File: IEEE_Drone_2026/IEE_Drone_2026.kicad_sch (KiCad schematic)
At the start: 15 parts, among them IC1 TPSM84209RKHT, J1 Conn_01x03_Socket, J2 Conn_01x03_Socket, J3 Conn_01x03_Socket, J4 Conn_01x03_Socket, U1 MS560702BA03-50

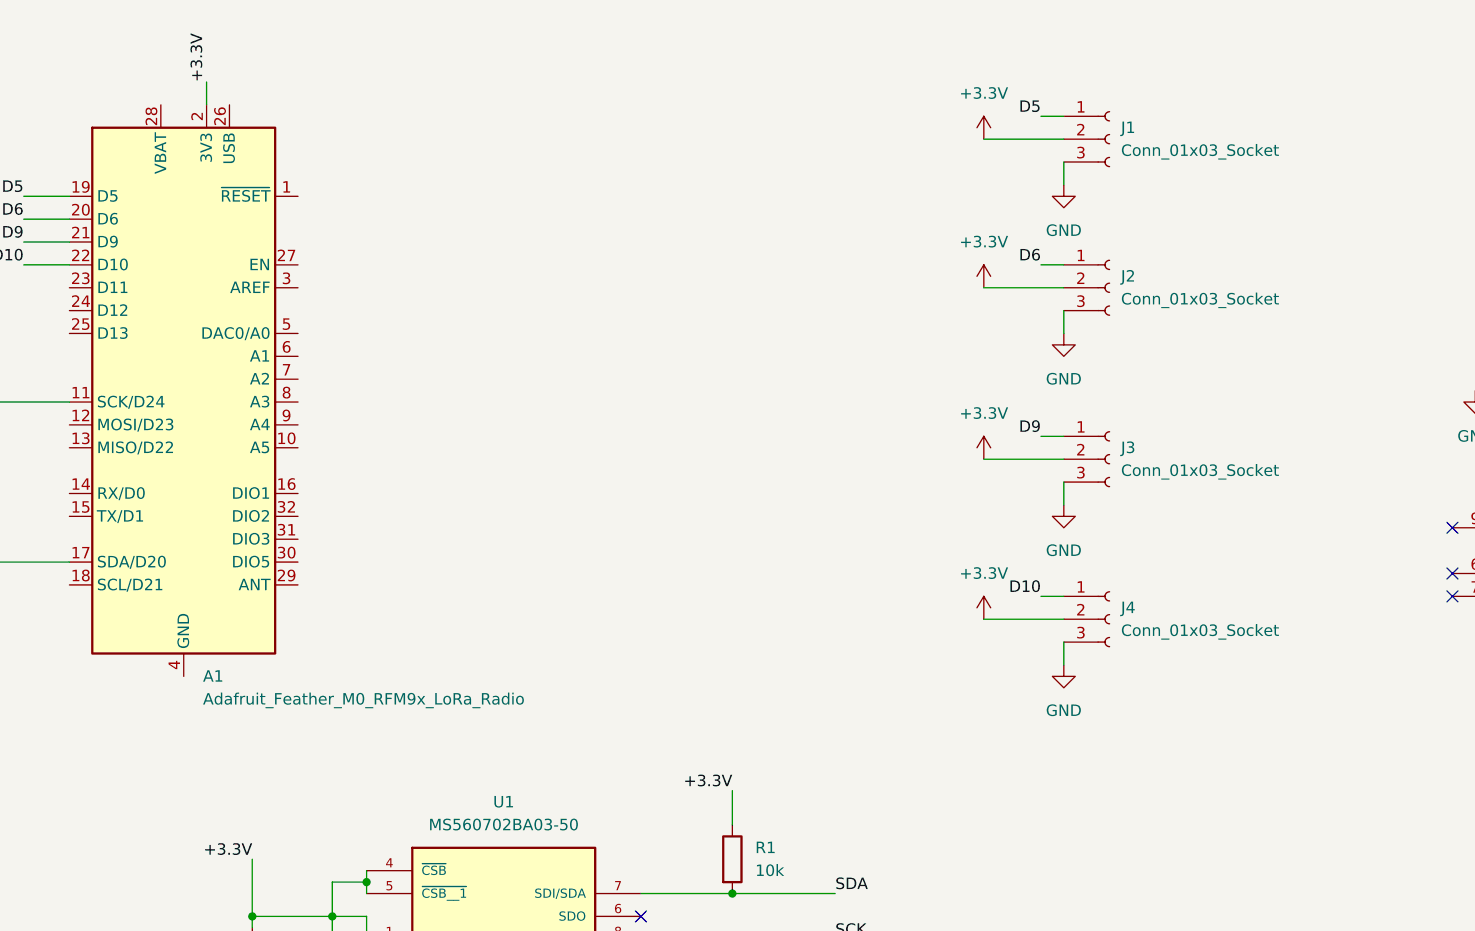
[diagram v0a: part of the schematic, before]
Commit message: redesign of feather system to incorporate ESC system
added mounting pins, changed board size, redesigned pwr system and moved it and barometer, removed individual servo pins and added 1x6 conn for ESC
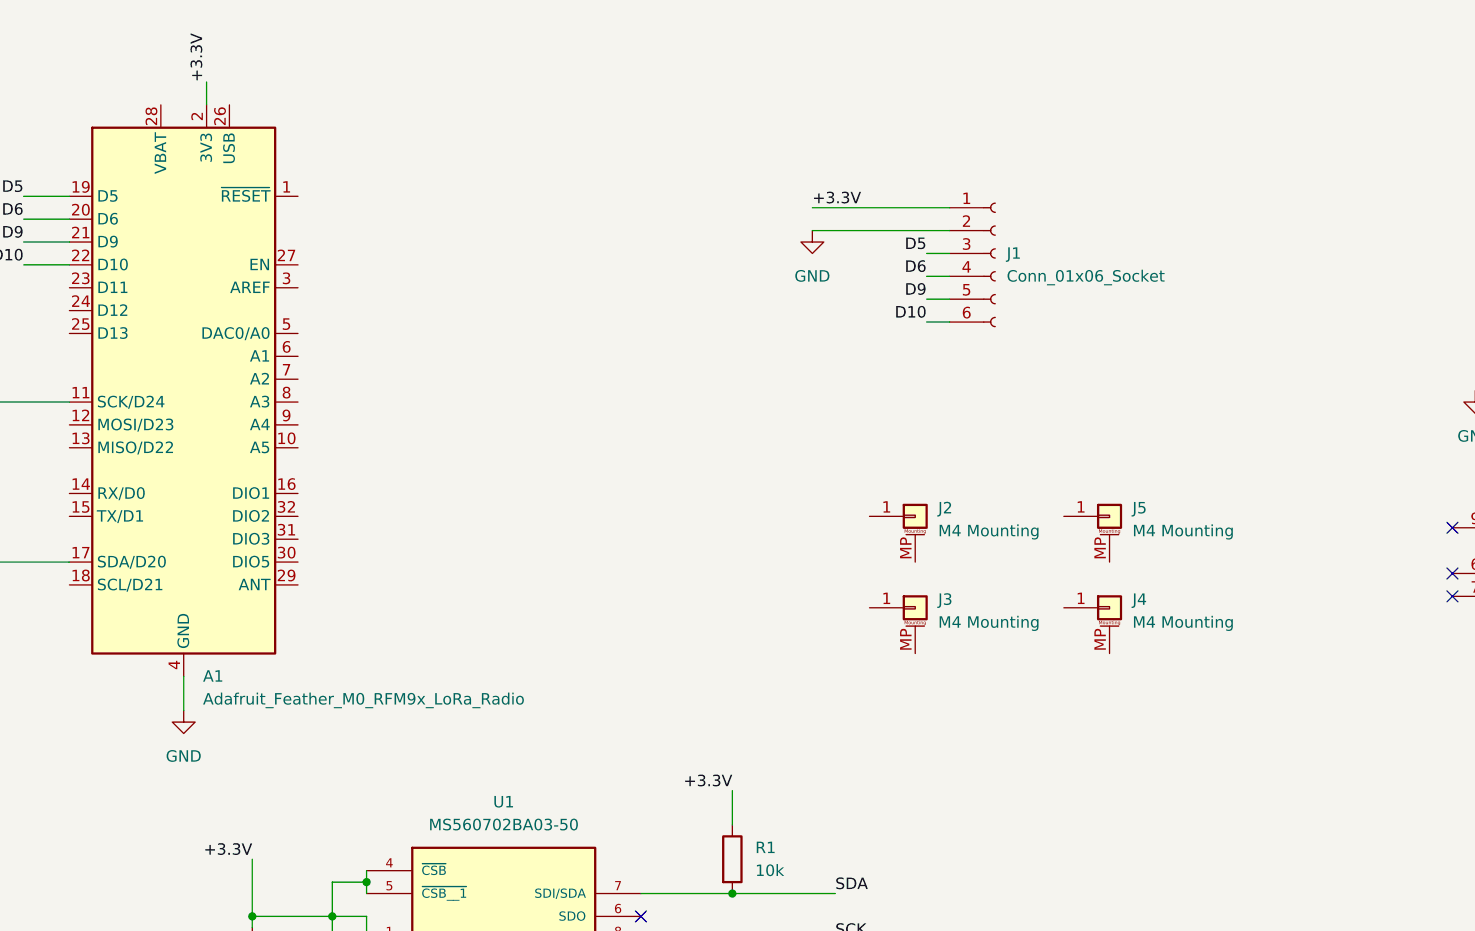
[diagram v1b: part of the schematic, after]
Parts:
- removed J1, J2, J3, J4: Conn_01x03_Socket, Connector_PinSocket_2.54mm:PinSocket_1x03_P2.54mm_Vertical, symbol Connector:Conn_01x03_Socket
- added J1: Conn_01x06_Socket, Connector_PinHeader_1.00mm:PinHeader_1x06_P1.00mm_Vertical, symbol Connector:Conn_01x06_Socket
- added J2, J3, J4, J5: M4 Mounting, Mounting:MountingHole_4.3mm_M4, symbol Connector_Generic_MountingPin:Conn_01x01_MountingPin
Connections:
- net +3.3V: now also J1.1 (Pin_1)
- net D10: now also J1.6 (Pin_6)
- net D5: now also J1.3 (Pin_3)
- net D6: now also J1.4 (Pin_4)
- net D9: now also J1.5 (Pin_5)
- net GND: now also A1.4 (GND), J1.2 (Pin_2)

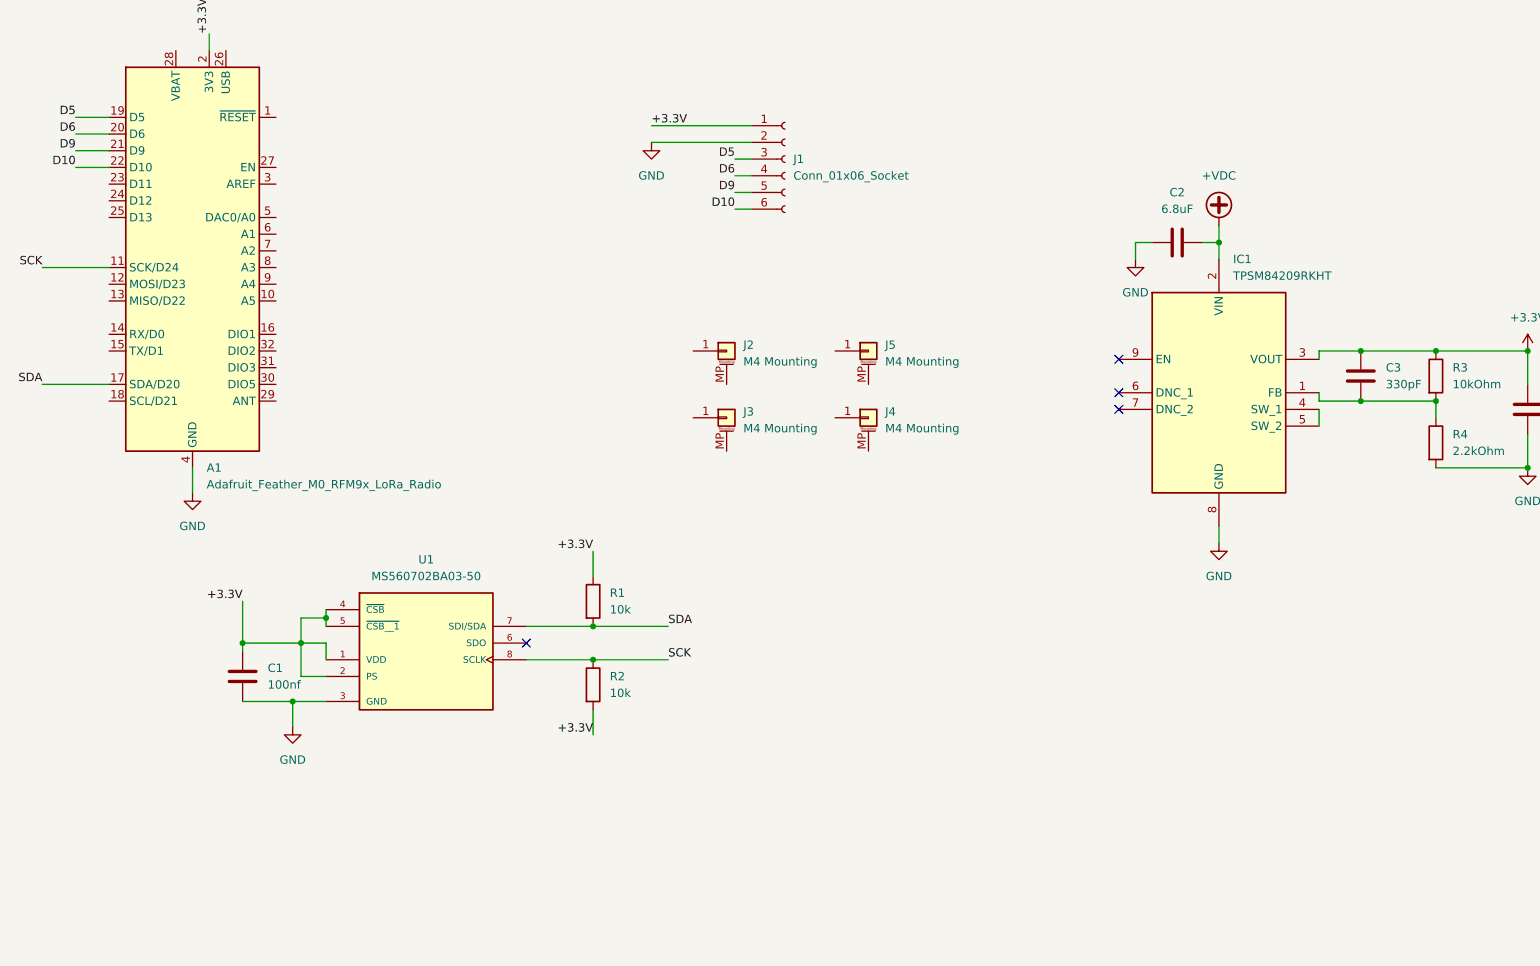
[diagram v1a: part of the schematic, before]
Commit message: added second power regulator for 6v to pixy2m added a couple more labels
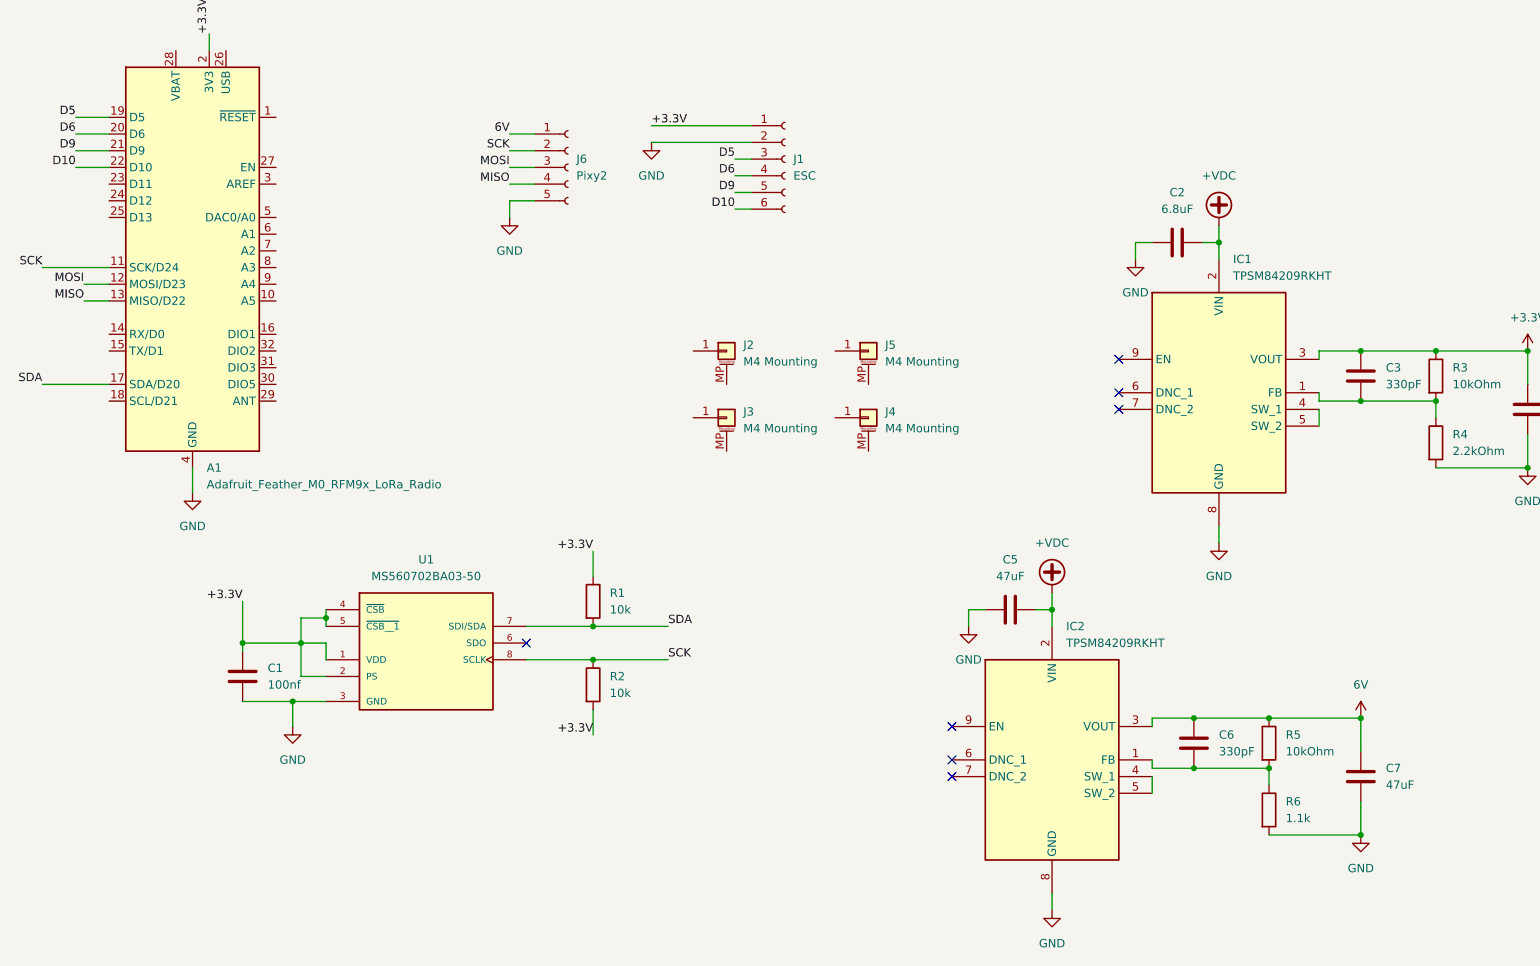
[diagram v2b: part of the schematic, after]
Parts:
- added C5, C7: 47uF, Capacitor_SMD:C_0603_1608Metric_Pad1.08x0.95mm_HandSolder, symbol Device:C
- added C6: 330pF, Capacitor_SMD:C_0603_1608Metric_Pad1.08x0.95mm_HandSolder, symbol Device:C
- added IC2: TPSM84209RKHT, TPSM84209RKHT, symbol TPSM84209RKHT:TPSM84209RKHT
- added J6: Pixy2, Connector_PinSocket_2.54mm:PinSocket_1x05_P2.54mm_Vertical, symbol Connector:Conn_01x05_Socket
- added R5: 10kOhm, Resistor_SMD:R_0603_1608Metric_Pad0.98x0.95mm_HandSolder, symbol Device:R
- added R6: 1.1k, Resistor_SMD:R_0603_1608Metric_Pad0.98x0.95mm_HandSolder, symbol Device:R
- J1: value Conn_01x06_Socket -> ESC
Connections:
- net +VDC: now also C5.2, IC2.2 (VIN)
- net GND: now also C5.1, C7.2, IC2.8 (GND), J6.5 (Pin_5), R6.2
- net SCK: now also J6.2 (Pin_2)
- net MOSI: now reaches A1.12 (MOSI/D23)
- net MOSI: now also J6.3 (Pin_3)
- net MISO: now reaches A1.13 (MISO/D22)
- net MISO: now also J6.4 (Pin_4)
- new net: C6.2, IC2.1 (FB), R5.2, R6.1
- new net: IC2.4 (SW_1), IC2.5 (SW_2)
- new net 6V: C6.1, C7.1, IC2.3 (VOUT), J6.1 (Pin_1), R5.1
- no-connect marks 4 -> 7

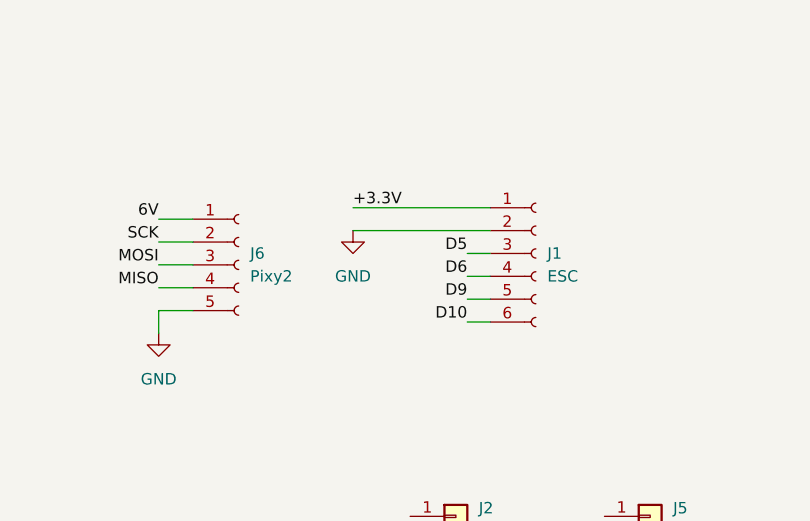
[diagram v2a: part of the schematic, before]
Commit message: updated ESC connector to fix conn issue.
will need to twist the ESC connection cable to properly connect to the ESC
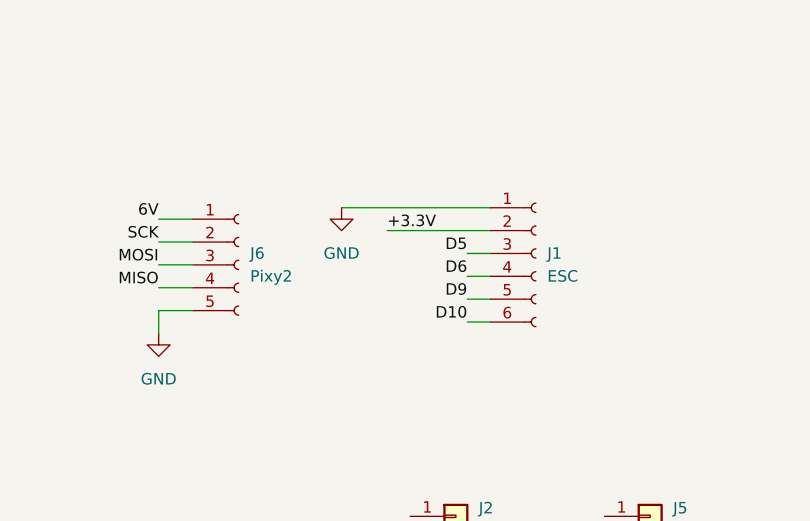
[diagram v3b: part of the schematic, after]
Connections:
- net +3.3V: now also J1.2 (Pin_2); no longer J1.1 (Pin_1)
- net GND: now also J1.1 (Pin_1); no longer J1.2 (Pin_2)
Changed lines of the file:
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@@
+	(wire
+		(pts
+			(xy 146.05 38.1) (xy 157.48 38.1)
+		)
+		(stroke
+			(width 0)
+			(type default)
+		)
+	)
 	(wire
 		(pts
@@
 	(wire
 		(pts
-			(xy 142.24 38.1) (xy 157.48 38.1)
-		)
-		(stroke
-			(width 0)
-			(type default)
-		)
-	)
-	(wire
-		(pts
 			(xy 120.65 46.99) (xy 124.46 46.99)
 		)
@@
 	(wire
 		(pts
+			(xy 140.97 35.56) (xy 157.48 35.56)
+		)
+		(stroke
+			(width 0)
+			(type default)
+		)
+	)
+	(wire
+		(pts
 			(xy 72.39 87.63) (xy 72.39 91.44)
 		)
@@
 		(pts
 			(xy 133.35 111.76) (xy 144.78 111.76)
-		)
-		(stroke
-			(width 0)
-			(type default)
-		)
-	)
-	(wire
-		(pts
-			(xy 142.24 35.56) (xy 157.48 35.56)
 		)
 		(stroke
@@
 	)
 	(label "+3.3V"
-		(at 142.24 35.56 0)
+		(at 146.05 38.1 0)
 		(effects
 			(font
@@
 	(symbol
 		(lib_id "power:GND")
-		(at 142.24 38.1 0)
+		(at 140.97 35.56 0)
 		(unit 1)
 		(exclude_from_sim no)
@@
 		(fields_autoplaced yes)
 		(property "Reference" "#PWR02"
-			(at 142.24 44.45 0)
+			(at 140.97 41.91 0)
 			(effects
 				(font
@@
 		)
 		(property "Value" "GND"
-			(at 142.24 43.18 0)
+			(at 140.97 40.64 0)
 			(effects
 				(font
@@
 		)
 		(property "Footprint" ""
-			(at 142.24 38.1 0)
+			(at 140.97 35.56 0)
 			(effects
 				(font
@@
 		)
 		(property "Datasheet" ""
-			(at 142.24 38.1 0)
+			(at 140.97 35.56 0)
 			(effects
 				(font
@@
 		)
 		(property "Description" "Power symbol creates a global label with name \"GND\" , ground"
-			(at 142.24 38.1 0)
-			(effects
-				(font
+			(at 140.97 35.56 0)
+			(effects
+				(font

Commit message: added crappy mounting holes. probably need to redo
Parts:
- added J10, J7, J8, J9: M2, MountingHole:MountingHole_2.2mm_M2, symbol Connector_Generic_MountingPin:Conn_01x01_MountingPin
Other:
- moved on the sheet: J2, J3, J4, J5

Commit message: designed transistor circuit & pcb
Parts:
- added J11: Conn_01x02_Socket, Connector_PinHeader_2.54mm:PinHeader_1x02_P2.54mm_Vertical, symbol Connector:Conn_01x02_Socket
- added Q1: 2N2222, Package_TO_SOT_THT:TO-39-3, symbol Transistor_BJT:2N2219
- added R7: 300, Resistor_SMD:R_0603_1608Metric_Pad0.98x0.95mm_HandSolder, symbol Device:R
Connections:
- net +3.3V: now also J11.1 (Pin_1)
- net GND: now also Q1.1 (E)
- net D11: now reaches A1.23 (D11)
- net D11: now also R7.1
- new net: J11.2 (Pin_2), Q1.3 (C)
- new net: Q1.2 (B), R7.2
